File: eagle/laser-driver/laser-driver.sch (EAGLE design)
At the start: 49 parts, among them IC1 74HC589D, IC2 74HC589D, IC3 TC7660SOIC8, T1 2N7002E, T2 2N7002E, U1 AD8041ARZ, U2 SN74HC163NSR, U3 SN74LVC1G14DBVT, U4 MCP6291T-E/OT, U5 SN74AHCT1G08DCKR, U6 SN74LVC1G17DBVR

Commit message: Update PCBs, schematics, processed jobs, etc.
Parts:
- removed D1: VTB8441BH, mulabs:VTB8441BH
- removed U1: AD8041ARZ, Analog Devices_By_element14_Batch_1:AD8041ARZ
- removed U3: SN74LVC1G14DBVT, Texas Instruments_By_element14_Batch_1:SN74LVC1G14DBVT
- removed U4: MCP6291T-E/OT, Microchip_By_element14_Batch_1:MCP6291T-E/OT
- removed U5: SN74AHCT1G08DCKR, Texas Instruments_By_element14_Batch_1:SN74AHCT1G08DCKR
- removed U6: SN74LVC1G17DBVR, Texas Instruments_By_element14_Batch_1:SN74LVC1G17DBVR
- added C14, C15, C16, C18, C20, C24: 10nF, rcl:C-EUC1206
- added C17, C19, C23: 1µ, rcl:C-EUC1206
- added C21: 100nF, rcl:C-EUC1206
- added C22: 10µ, rcl:CPOL-EUA/3216-18R
- added C25: 100µF, rcl:CPOL-EUD/7343-31R
- added C26, C29, C30: 100nF, rcl:C-EUC0603
- added C27, C28: 220µ, rcl:CPOL-EU153CLV-0605
- added C31: 100n, rcl:C-EUC0603
- added C32: 22pF, rcl:C-EUC0603
- added COMP: TPB1,27, testpad:TPB1,27
- added D2: 15MQ040NTR, SparkFun:DIODE-SCHOTTKY_
- added D3: VTB8441BH, mulabs:VTB8441BH
- added IC4: AD8041R, analog-devices:AD8041R
- added IC5: 74LVC1G17DBV, 74xx-little-de:74LVC1G17DBV
- added IC6: 74LVC1G14DBV, 74xx-little-de:74LVC1G14DBV
- added IC7: 74AHCT1G08DCK, 74xx-little-de:74AHCT1G08DCK
- added LED1, LED2: (no value), led:LEDCHIPLED_0805
- added R16: 820Ω, rcl:R-EU_R0603
- added R17: 10kΩ, rcl:R-EU_R0603
- added R18: 270Ω, rcl:R-EU_R0603
- added R19: 10k, rcl:R-EU_R0603
- added R20: 100k, pot:TRIM_EU-SM-42/43B
- added R21: 100kΩ+, rcl:R-EU_R0603
- added R22, R23: 300Ω, rcl:R-EU_R0603
- added R24: 1kΩ, pot:TRIM_EU-3223G
- added SJ1: CURRENT MEASURE, SparkFun:SOLDERJUMPERNO
- added T3: 2N7002E, nxp_60:2N7002E
- added TVS2: 6V, supressor:TVS-0805
- added U7: MCP6561T, mulabs:MCP6561T
- added U8: MCP6291T-E/OT, mulabs:MCP6291T-E/OT
- C13: device rcl:C-EUC1206 -> rcl:C-EUC0603
- C5: value 100pF -> 10nF; device rcl:C-EUC1206 -> rcl:C-EUC0603
- C6, C7: value 50pF -> 10nF
- R1, R12, R4, R9: device rcl:R-EU_R1206 -> rcl:R-EU_R0603
- R13: value 1k -> 10k; device rcl:R-EU_R1206 -> rcl:R-EU_R0603
- R14: value 100k -> 150Ω; device rcl:R-EU_R1206 -> rcl:R-EU_R0603
- R2: value 120Ω -> 1kΩ; device rcl:R-EU_R1206 -> rcl:R-EU_R0603
- R3: value 5k -> 1kΩ; device pot:TRIM_EU-3223W -> pot:TRIM_EU-SM-42/43B
- R5: value 1k -> 5.1kΩ; device rcl:R-EU_R1206 -> rcl:R-EU_R0603
- R6: value 10Ω -> 12Ω; device rcl:R-EU_R1206 -> rcl:R-EU_R0603
- R7: value 3.3kΩ -> 100 Ω; device rcl:R-EU_R1206 -> rcl:R-EU_R0603
- R8: value 6.8kΩ -> 100 Ω; device rcl:R-EU_R1206 -> rcl:R-EU_R0603
- renumbered N(SYNC) to !RESET
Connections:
- new net N$13: C15.1, R1.1, R8.2, T2.G
- new net N$28: R16.1, T2.S
- new net N$29: R18.1, T3.S
- new net N$30: R13.2, R19.1, U8.IN+
- new net N$31: D2.C, SJ1.1, TVS2.2, U$1.1
- new net N$32: C5.1, PD.TP, R12.2, U7.IN-
- new net N$33: LED1.C, R22.2
- new net N$34: LED2.C, R23.2
- new net N$35: IC4.IN-, R2.2
- new net N$36: R14.2, R24.A
- net GND: now also C14.2, C15.2, C16.2, C17.2, C18.2, C19.2, C20.2, C22.+, C23.1, C24.1, C25.-, C26.2, C27.-, C28.-, C29.2, C30.2, C31.2, C32.2, C6.2, C7.2, IC5P.GND, IC6P.GND, IC7P.GND, R13.1, R16.2, R17.2, R18.2, R20.E, R22.1, R23.1, R3.E, U7.VCC-, U8.VCC-; no longer D1.A, R2.1, R3.A, T2.S, U3.GND, U4.VIN+, U5.GND, U6.GND
- net N$1: now also IC4.DISABLE; no longer U1.~DISABLE
- net N$12: now also R21.1, U7.OUT; no longer C5.1, PD.TP, R12.2
- net N$15: now also C21.2
- net N$16: now also IC7A.O; no longer U5.Y
- net N$17: now also IC6A.O, IC7A.I1; no longer U3.Y, U5.B
- net N$19: now also COMP.TP, R20.S, R21.2, U7.IN+; no longer C6.2, C7.2, R13.2, U4.VIN-
- net N$2: now also C32.1, R3.A, T3.D; no longer R2.2, R3.E
- net N$20: now also IC6A.I; no longer U3.A
- net N$21: now also D3.A, U8.IN-; no longer D1.K, R13.1
- net N$23: now also R24.E, R24.S, U8.OUT; no longer C6.1, C7.1, R14.2, U4.VOUT
- net N$24: now also IC5G$1.I; no longer U6.A
- net N$25: now also C21.1
- net N$27: now also IC5G$1.O, IC7A.I0; no longer U5.A, U6.Y
- net N$3: now also IC4.OUT; no longer U1.OUTPUT
- net N$5: now also D2.A, TVS2.1
- net N$6: now also R2.1; no longer U1.-INPUT
- net N$8: now also IC4.IN+; no longer U1.+INPUT
- net N$9: now also C14.1, R17.1, T3.G; no longer R1.1, R8.2, T2.G
- net VCC: now also C16.1, C17.1, C18.1, C19.1, C20.1, C25.+, C26.1, C27.+, C28.+, C29.1, C30.1, C31.1, C6.1, C7.1, D3.K, IC4.+VS, IC5P.VCC, IC6P.VCC, IC7P.VCC, LED1.A, LED2.A, R19.2, R20.A, SJ1.2, U7.VCC+, U8.VCC+; no longer U$1.1, U1.+VS, U3.VCC, U4.VDD, U5.VCC, U6.VCC
- net VSS: now also C22.-, C23.2, C24.2, IC4.-VS; no longer U1.-VS, U4.VSS
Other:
- note added: "0-5 V modulation"
- note added: "GND 1 2 +5 V DATA0 3 4 DATA1 DATA2 5 6 DATA3 DATA4 7 8 DATA5 DATA6 9 10 DATA7 LATCH RE 11 12 (OUT) PHOTODIODE DATA8 13 14 DATA9 DATA10 15 16 DATA11 DATA12 17 18 DATA13 DATA14 19 20 DATA15 CLK RE 21 22 (OUT) PREFETCH (LOAD NEXT WORD) PWR0 23 24 !SYNC (RESET COUNTER) PWR1 25 26 LASER ENABLE"
- note added: "PREFETCH"
- note removed: "0…5 V modulation"
- note removed: "LD-NEXT"
- moved on the sheet: C1, C11, C13, C2, C3, C5, C6, C7, C8, C9, CUR, IC1P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

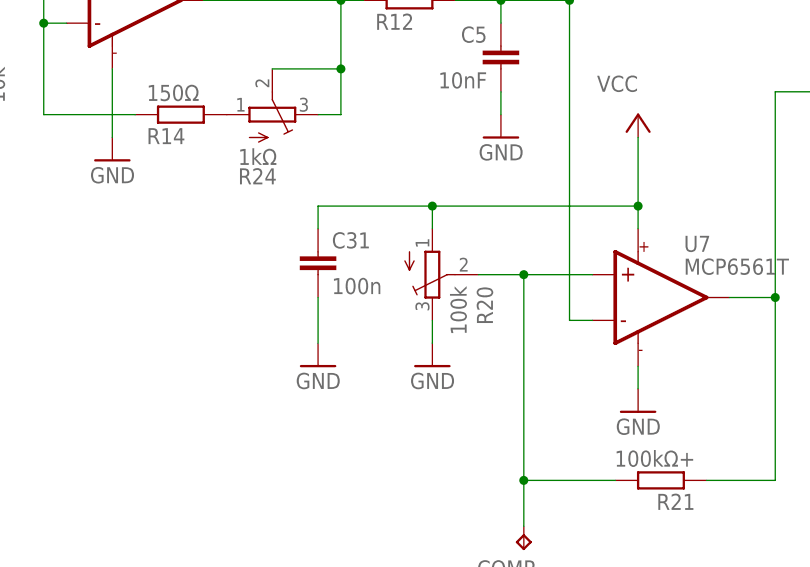
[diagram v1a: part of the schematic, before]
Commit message: PLL acquires lock
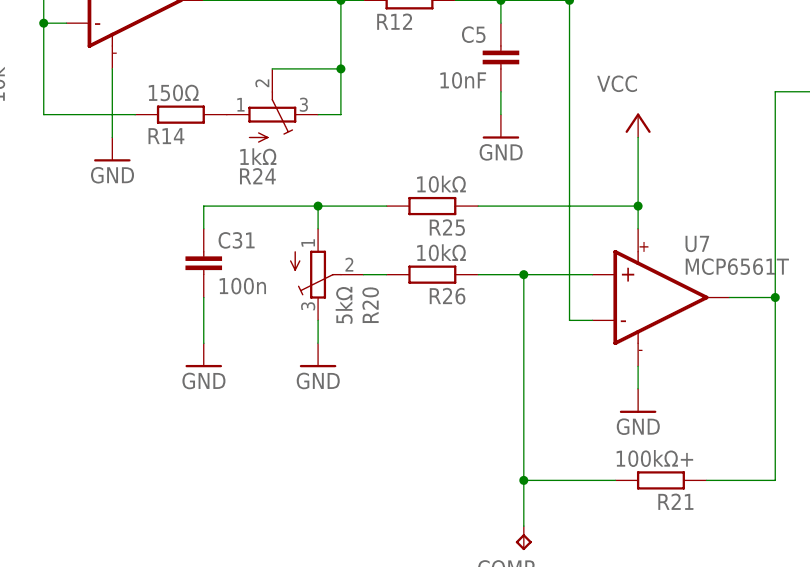
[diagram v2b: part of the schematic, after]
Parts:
- added R25, R26: 10kΩ, rcl:R-EU_R0603
- R20: value 100k -> 5kΩ
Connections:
- new net N$37: C31.1, R20.A, R25.2
- new net N$38: R20.S, R26.2
- net N$19: now also R26.1; no longer R20.S
- net VCC: now also R25.1; no longer C31.1, R20.A
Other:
- moved on the sheet: C31, R20
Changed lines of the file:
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@@
 <?xml version="1.0" encoding="utf-8"?>
 <!DOCTYPE eagle SYSTEM "eagle.dtd">
-<eagle version="7.5.0">
+<eagle version="7.7.0">
 <drawing>
 <settings>
@@
 <part name="C29" library="rcl" deviceset="C-EU" device="C0603" value="100nF"/>
 <part name="GND29" library="supply1" deviceset="GND" device=""/>
-<part name="R20" library="pot" deviceset="TRIM_EU-" device="SM-42/43B" value="100k"/>
+<part name="R20" library="pot" deviceset="TRIM_EU-" device="SM-42/43B" value="5kΩ"/>
 <part name="GND30" library="supply1" deviceset="GND" device=""/>
 <part name="GND31" library="supply1" deviceset="GND" device=""/>
@@
 <part name="R24" library="pot" deviceset="TRIM_EU-" device="3223G" value="1kΩ"/>
 <part name="COMP" library="testpad" deviceset="TP" device="B1,27"/>
+<part name="R25" library="rcl" deviceset="R-EU_" device="R0603" value="10kΩ"/>
+<part name="R26" library="rcl" deviceset="R-EU_" device="R0603" value="10kΩ"/>
 </parts>
 <sheets>
@@
 CLK RE      21    22       (OUT) PREFETCH (LOAD NEXT WORD)
 PWR0        23    24       !SYNC (RESET COUNTER)
-PWR1        25    26       LASER ENABLE
-</text>
+PWR1        25    26       LASER ENABLE</text>
 </plain>
 <instances>
@@
 </instance>
 <instance part="GND29" gate="1" x="33.02" y="86.36" rot="MR0"/>
-<instance part="R20" gate="1" x="55.88" y="45.72" smashed="yes" rot="MR180">
-<attribute name="NAME" x="62.611" y="44.45" size="1.778" layer="95" rot="MR270"/>
-<attribute name="VALUE" x="59.69" y="44.45" size="1.778" layer="96" rot="MR270"/>
+<instance part="R20" gate="1" x="43.18" y="45.72" smashed="yes" rot="MR180">
+<attribute name="NAME" x="49.911" y="44.45" size="1.778" layer="95" rot="MR270"/>
+<attribute name="VALUE" x="46.99" y="44.45" size="1.778" layer="96" rot="MR270"/>
 </instance>
 <instance part="GND30" gate="1" x="78.74" y="30.48" rot="MR0"/>
-<instance part="GND31" gate="1" x="55.88" y="35.56" rot="MR0"/>
+<instance part="GND31" gate="1" x="43.18" y="35.56" rot="MR0"/>
 <instance part="P+12" gate="VCC" x="78.74" y="63.5" smashed="yes" rot="MR0">
 <attribute name="VALUE" x="78.74" y="66.04" size="1.778" layer="96" rot="MR0"/>
 </instance>
-<instance part="GND32" gate="1" x="43.18" y="35.56" rot="MR0"/>
-<instance part="C31" gate="G$1" x="43.18" y="48.26"/>
+<instance part="GND32" gate="1" x="30.48" y="35.56" rot="MR0"/>
+<instance part="C31" gate="G$1" x="30.48" y="48.26"/>
 <instance part="C30" gate="G$1" x="254" y="177.8"/>
 <instance part="R21" gate="G$1" x="81.28" y="22.86" rot="R180"/>
@@
 <instance part="R24" gate="1" x="38.1" y="63.5" rot="MR90"/>
 <instance part="COMP" gate="G$1" x="66.04" y="15.24" rot="R180"/>
+<instance part="R25" gate="G$1" x="55.88" y="53.34" rot="R180"/>
+<instance part="R26" gate="G$1" x="55.88" y="45.72" rot="R180"/>
 </instances>
 <busses>
@@
 </segment>
 <segment>
+<pinref part="U7" gate="G$1" pin="VCC+"/>
+<wire x1="78.74" y1="53.34" x2="78.74" y2="50.8" width="0.1524" layer="91"/>
 <pinref part="P+12" gate="VCC" pin="VCC"/>
-<wire x1="43.18" y1="50.8" x2="43.18" y2="53.34" width="0.1524" layer="91"/>
-<pinref part="C31" gate="G$1" pin="1"/>
-<pinref part="U7" gate="G$1" pin="VCC+"/>
-<wire x1="43.18" y1="53.34" x2="55.88" y2="53.34" width="0.1524" layer="91"/>
-<wire x1="55.88" y1="53.34" x2="78.74" y2="53.34" width="0.1524" layer="91"/>
-<wire x1="78.74" y1="53.34" x2="78.74" y2="50.8" width="0.1524" layer="91"/>
 <wire x1="78.74" y1="60.96" x2="78.74" y2="53.34" width="0.1524" layer="91"/>
 <junction x="78.74" y="53.34"/>
-<pinref part="R20" gate="1" pin="A"/>
-<wire x1="55.88" y1="50.8" x2="55.88" y2="53.34" width="0.1524" layer="91"/>
-<junction x="55.88" y="53.34"/>
+<wire x1="60.96" y1="53.34" x2="78.74" y2="53.34" width="0.1524" layer="91"/>
+<pinref part="R25" gate="G$1" pin="1"/>
 </segment>
 <segment>
@@
 </segment>
 <segment>
-<wire x1="43.18" y1="43.18" x2="43.18" y2="38.1" width="0.1524" layer="91"/>
+<wire x1="30.48" y1="43.18" x2="30.48" y2="38.1" width="0.1524" layer="91"/>
 <pinref part="GND32" gate="1" pin="GND"/>
 <pinref part="C31" gate="G$1" pin="2"/>
@@
 <pinref part="R20" gate="1" pin="E"/>
 <pinref part="GND31" gate="1" pin="GND"/>
-<wire x1="55.88" y1="40.64" x2="55.88" y2="38.1" width="0.1524" layer="91"/>
+<wire x1="43.18" y1="40.64" x2="43.18" y2="38.1" width="0.1524" layer="91"/>
 </segment>
 </net>
@@
 <net name="N$19" class="0">
 <segment>
-<pinref part="R20" gate="1" pin="S"/>
 <wire x1="66.04" y1="45.72" x2="60.96" y2="45.72" width="0.1524" layer="91"/>
 <junction x="66.04" y="45.72"/>
@@
 <wire x1="66.04" y1="17.78" x2="66.04" y2="22.86" width="0.1524" layer="91"/>
 <junction x="66.04" y="22.86"/>
+<pinref part="R26" gate="G$1" pin="1"/>
 </segment>
 </net>
@@
 </segment>
 </net>
+<net name="N$37" class="0">
+<segment>
+<wire x1="30.48" y1="50.8" x2="30.48" y2="53.34" width="0.1524" layer="91"/>
+<pinref part="C31" gate="G$1" pin="1"/>
+<wire x1="30.48" y1="53.34" x2="43.18" y2="53.34" width="0.1524" layer="91"/>
+<wire x1="43.18" y1="53.34" x2="50.8" y2="53.34" width="0.1524" layer="91"/>
+<pinref part="R20" gate="1" pin="A"/>
+<wire x1="43.18" y1="50.8" x2="43.18" y2="53.34" width="0.1524" layer="91"/>
+<junction x="43.18" y="53.34"/>
+<pinref part="R25" gate="G$1" pin="2"/>
+</segment>
+</net>
+<net name="N$38" class="0">
+<segment>
+<pinref part="R20" gate="1" pin="S"/>
+<pinref part="R26" gate="G$1" pin="2"/>
+<wire x1="50.8" y1="45.72" x2="48.26" y2="45.72" width="0.1524" layer="91"/>
+</segment>
+</net>
